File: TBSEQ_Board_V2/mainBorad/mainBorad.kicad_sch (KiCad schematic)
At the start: 0 parts

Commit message: mainBoard
VCO
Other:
- added sheet AnVCO (VCO.kicad_sch)
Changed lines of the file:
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@@
+	)
+	(sheet
+		(at 102.87 57.15)
+		(size 20.32 7.62)
+		(fields_autoplaced yes)
+		(stroke
+			(width 0.1524)
+			(type solid)
+		)
+		(fill
+			(color 0 0 0 0.0000)
+		)
+		(property "Sheetname" "AnVCO"
+			(at 102.87 56.4384 0)
+			(effects
+				(font
+					(size 1.27 1.27)
+				)
+				(justify left bottom)
+			)
+		)
+		(property "Sheetfile" "VCO.kicad_sch"
+			(at 102.87 65.3546 0)
+			(effects
+				(font
+					(size 1.27 1.27)
+				)
+				(justify left top)
+			)
+		)
+		(instances
+			(project "mainBorad"
+				(path "/74b57c73-2ea6-4d1a-baa5-ad46186fbb51"
+					(page "10")
+				)
+			)
+		)
 	)
 	(sheet

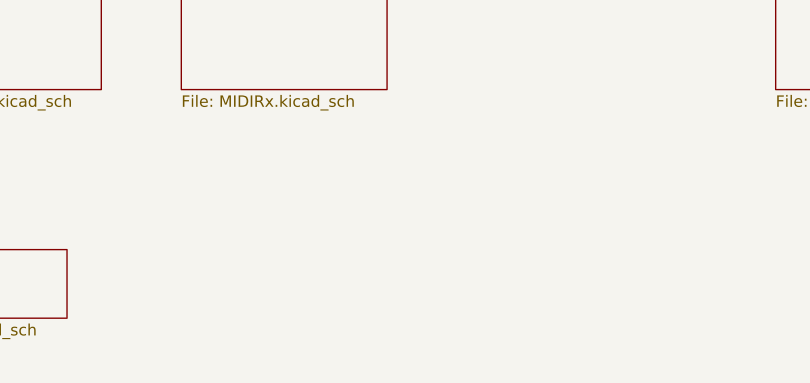
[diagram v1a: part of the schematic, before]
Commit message: mainboard
部品を全部配置しただけ
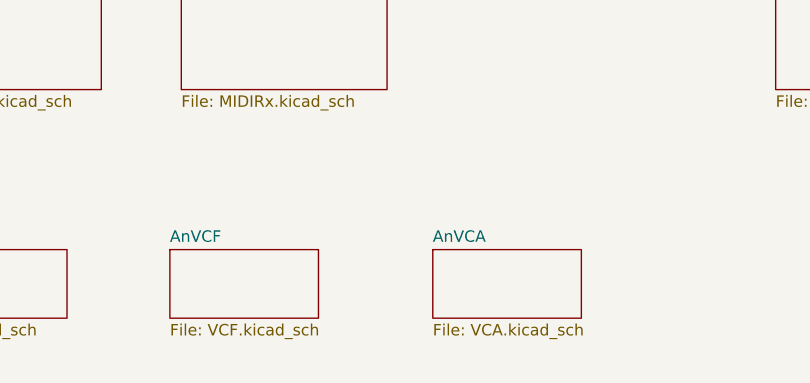
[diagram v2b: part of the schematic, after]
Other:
- added sheet AnVCA (VCA.kicad_sch)
- added sheet AnVCF (VCF.kicad_sch)
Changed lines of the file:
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@@
+	)
+	(sheet
+		(at 134.62 57.15)
+		(size 16.51 7.62)
+		(fields_autoplaced yes)
+		(stroke
+			(width 0.1524)
+			(type solid)
+		)
+		(fill
+			(color 0 0 0 0.0000)
+		)
+		(property "Sheetname" "AnVCF"
+			(at 134.62 56.4384 0)
+			(effects
+				(font
+					(size 1.27 1.27)
+				)
+				(justify left bottom)
+			)
+		)
+		(property "Sheetfile" "VCF.kicad_sch"
+			(at 134.62 65.3546 0)
+			(effects
+				(font
+					(size 1.27 1.27)
+				)
+				(justify left top)
+			)
+		)
+		(instances
+			(project "mainBorad"
+				(path "/74b57c73-2ea6-4d1a-baa5-ad46186fbb51"
+					(page "11")
+				)
+			)
+		)
 	)
 	(sheet
@@
 				)
 			)
+		)
+	)
+	(sheet
+		(at 163.83 57.15)
+		(size 16.51 7.62)
+		(fields_autoplaced yes)
+		(stroke
+			(width 0.1524)
+			(type solid)
+		)
+		(fill
+			(color 0 0 0 0.0000)
+		)
+		(property "Sheetname" "AnVCA"
+			(at 163.83 56.4384 0)
+			(effects
+				(font
+					(size 1.27 1.27)
+				)
+				(justify left bottom)
+			)
+		)
+		(property "Sheetfile" "VCA.kicad_sch"
+			(at 163.83 65.3546 0)
+			(effects
+				(font
+					(size 1.27 1.27)
+				)
+				(justify left top)
+			)
+		)
+		(instances
+			(project "mainBorad"
+				(path "/74b57c73-2ea6-4d1a-baa5-ad46186fbb51"
+					(page "12")
+				)
+			)
